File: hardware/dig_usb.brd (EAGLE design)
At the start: 146.1 x 102.6 mm, 157 parts, among them IC1 AT90USB1287-AU, IC202 DS1337S, IC203 MAX487CSA, IC204 74HC166D, IC301 LTV-356T, IC302 LTV-356T, IC303 LTV-356T, IC304 LTV-356T, IC305 LTV-356T, IC306 LTV-356T, IC307 LTV-356T, IC308 LTV-356T, K401 S202S02, K402 S202S02, K403 S202S02, K404 S202S02, K405 S202S02, K406 S202S02, K407 S202S02, K408 S202S02, Q1 16MHz, Q201 32,768kHz, T301 BCR191, T302 BCR191, T303 BCR191, T304 BCR191, T305 BCR191, T306 BCR191, T307 BCR191, T308 BCR191, X101 RIA-73-02, X201 ISP, X202 RIA-73-02, X301 RIA-73-02, X302 RIA-73-02, X303 RIA-73-02, X304 RIA-73-02, X305 RIA-73-02, X401 RIA-73-02, X402 RIA-73-02, X403 RIA-73-02, X404 RIA-73-02, X405 RIA-73-02

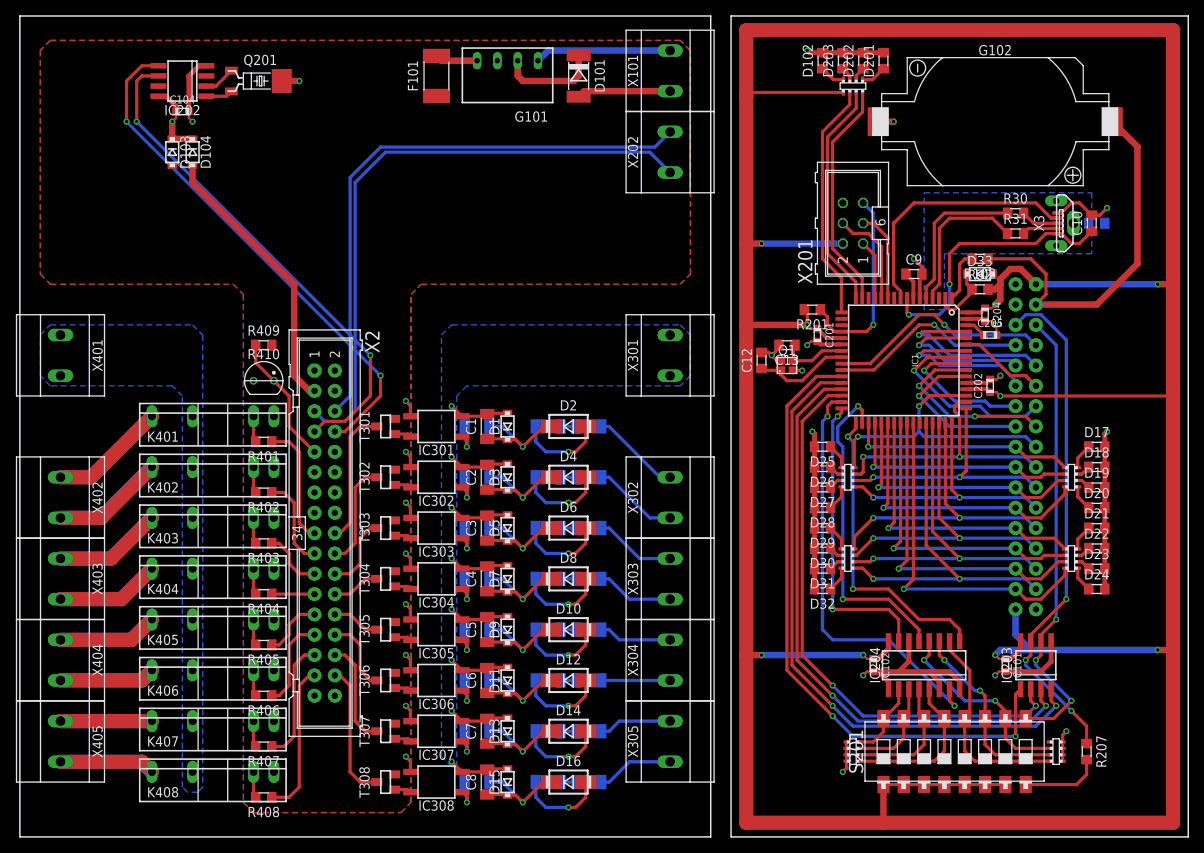
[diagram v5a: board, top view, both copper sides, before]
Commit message: Padgröße bei Wannenstecker für dig_usb angepasst
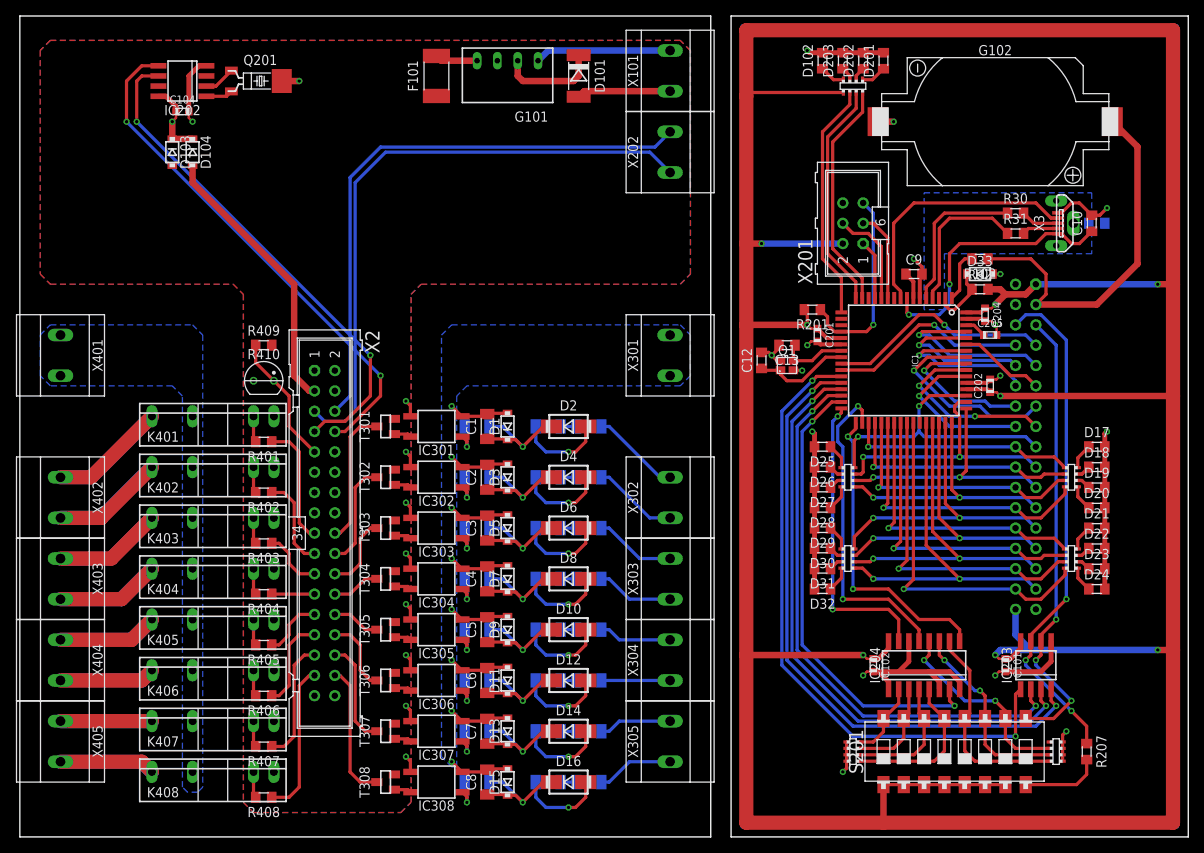
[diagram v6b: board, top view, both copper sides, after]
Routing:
- net C1: track 52.9 -> 57.6 mm
- net +5V: track 474.8 -> 472.4 mm, vias 9 -> 8
- net RXD: track 79.5 -> 80.0 mm
- net TE: track 74.8 -> 75.3 mm
- net RE: track 70.7 -> 71.2 mm
- net TXD: track 79.0 -> 79.5 mm
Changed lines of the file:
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@@
 <contactref element="X2" pad="33"/>
 <contactref element="D33" pad="A"/>
-<wire x1="121.665" y1="69.85" x2="120.65" y2="69.85" width="0.4064" layer="1"/>
-<via x="120.65" y="69.85" extent="1-16" drill="0.4"/>
+<wire x1="121.665" y1="69.85" x2="122.555" y2="69.85" width="0.4064" layer="1"/>
+<via x="122.555" y="69.85" extent="1-16" drill="0.4"/>
 <contactref element="X2" pad="4"/>
 <contactref element="G102" pad="-"/>
@@
 <wire x1="105.88" y1="21.755" x2="105.41" y2="22.225" width="0.3048" layer="1"/>
 <via x="121.92" y="22.225" extent="1-16" drill="0.4"/>
-<via x="105.41" y="22.225" extent="1-16" drill="0.4"/>
 <wire x1="90.805" y1="100.33" x2="144.145" y2="100.33" width="1.778" layer="1"/>
 <wire x1="144.145" y1="100.33" x2="144.145" y2="68.58" width="1.778" layer="1"/>
@@
 <wire x1="120.135" y1="65.055" x2="120.65" y2="65.57" width="0.508" layer="1"/>
 <contactref element="R29" pad="4B"/>
-<wire x1="105.41" y1="22.225" x2="92.71" y2="22.225" width="0.8128" layer="16"/>
-<wire x1="92.71" y1="22.225" x2="90.805" y2="22.225" width="0.8128" layer="1"/>
-<via x="92.71" y="22.225" extent="1-16" drill="0.4"/>
+<wire x1="105.41" y1="22.225" x2="90.805" y2="22.225" width="0.8128" layer="1"/>
 <wire x1="121.92" y1="22.225" x2="122.555" y2="22.86" width="0.8128" layer="16"/>
 <wire x1="122.555" y1="22.86" x2="126.365" y2="22.86" width="0.8128" layer="16"/>
@@
 <contactref element="D103" pad="A"/>
 <wire x1="124.46" y1="24.765" x2="124.46" y2="27.94" width="0.8128" layer="16"/>
-<wire x1="127" y1="68.58" x2="125.095" y2="70.485" width="0.8128" layer="1"/>
-<wire x1="125.095" y1="70.485" x2="123.825" y2="70.485" width="0.8128" layer="1"/>
-<wire x1="123.825" y1="70.485" x2="122.555" y2="69.215" width="0.8128" layer="1"/>
-<wire x1="122.555" y1="69.215" x2="122.555" y2="68.58" width="0.8128" layer="1"/>
-<wire x1="122.555" y1="68.58" x2="122.555" y2="66.675" width="0.8128" layer="1"/>
-<wire x1="122.555" y1="66.675" x2="121.92" y2="66.04" width="0.8128" layer="1"/>
-<wire x1="121.015" y1="67.945" x2="121.92" y2="67.945" width="0.8128" layer="1"/>
-<wire x1="121.92" y1="67.945" x2="122.555" y2="68.58" width="0.8128" layer="1"/>
+<wire x1="123.19" y1="67.31" x2="121.92" y2="66.04" width="0.8128" layer="1"/>
 <wire x1="144.145" y1="68.58" x2="142.24" y2="68.58" width="0.8128" layer="1"/>
 <via x="142.24" y="68.58" extent="1-16" drill="0.4"/>
 <wire x1="142.24" y1="68.58" x2="127" y2="68.58" width="0.8128" layer="16"/>
-<wire x1="122.555" y1="54.61" x2="144.145" y2="54.61" width="0.4064" layer="1"/>
+<wire x1="122.555" y1="54.61" x2="144.145" y2="54.61" width="0.8128" layer="1"/>
 <wire x1="122.085" y1="55.08" x2="122.555" y2="54.61" width="0.3048" layer="1"/>
 <polygon width="0.4064" layer="1">
@@
 <vertex x="26.67" y="68.58"/>
 </polygon>
+<wire x1="123.19" y1="67.31" x2="125.73" y2="67.31" width="0.8128" layer="1"/>
+<wire x1="125.73" y1="67.31" x2="127" y2="68.58" width="0.8128" layer="1"/>
+<wire x1="121.015" y1="67.945" x2="122.555" y2="67.945" width="0.8128" layer="1"/>
+<wire x1="122.555" y1="67.945" x2="123.19" y2="67.31" width="0.8128" layer="1"/>
+<via x="105.41" y="22.225" extent="1-16" drill="0.4"/>
 <wire x1="52.07" y1="92.115" x2="90.805" y2="92.075" width="0" layer="19" extent="1-1"/>
 </signal>
@@
 <contactref element="IC204" pad="7"/>
 <contactref element="IC1" pad="31"/>
-<via x="100.965" y="52.07" extent="1-16" drill="0.4"/>
-<wire x1="100.965" y1="52.07" x2="100.33" y2="51.435" width="0.4064" layer="16"/>
-<wire x1="100.33" y1="51.435" x2="100.33" y2="25.4" width="0.4064" layer="16"/>
-<wire x1="100.33" y1="25.4" x2="101.6" y2="24.13" width="0.4064" layer="16"/>
-<wire x1="101.6" y1="24.13" x2="108.585" y2="24.13" width="0.4064" layer="16"/>
+<via x="99.06" y="51.435" extent="1-16" drill="0.4"/>
 <via x="116.84" y="15.875" extent="1-16" drill="0.4"/>
 <wire x1="116.84" y1="15.875" x2="116.205" y2="16.51" width="0.4064" layer="1"/>
 <wire x1="116.205" y1="16.51" x2="116.205" y2="17.955" width="0.4064" layer="1"/>
 <wire x1="102.69" y1="53.855" x2="101.48" y2="53.855" width="0.4064" layer="1"/>
-<wire x1="101.48" y1="53.855" x2="100.965" y2="53.34" width="0.4064" layer="1"/>
-<wire x1="100.965" y1="53.34" x2="100.965" y2="52.07" width="0.4064" layer="1"/>
-<wire x1="108.585" y1="24.13" x2="116.84" y2="15.875" width="0.4064" layer="16"/>
+<wire x1="101.48" y1="53.855" x2="99.06" y2="51.435" width="0.4064" layer="1"/>
+<wire x1="99.06" y1="51.435" x2="97.79" y2="50.165" width="0.4064" layer="16"/>
+<wire x1="97.79" y1="50.165" x2="97.79" y2="23.495" width="0.4064" layer="16"/>
+<wire x1="97.79" y1="23.495" x2="105.41" y2="15.875" width="0.4064" layer="16"/>
+<wire x1="105.41" y1="15.875" x2="116.84" y2="15.875" width="0.4064" layer="16"/>
 </signal>
 <signal name="!R">
@@
 <wire x1="128.905" y1="16.51" x2="129.54" y2="15.875" width="0.4064" layer="1"/>
 <via x="129.54" y="15.875" extent="1-16" drill="0.4"/>
-<wire x1="96.52" y1="20.955" x2="101.6" y2="15.875" width="0.4064" layer="1"/>
-<via x="101.6" y="15.875" extent="1-16" drill="0.4"/>
-<wire x1="101.6" y1="15.875" x2="104.14" y2="13.335" width="0.4064" layer="16"/>
+<wire x1="95.885" y1="21.59" x2="104.14" y2="13.335" width="0.4064" layer="16"/>
 <wire x1="104.14" y1="13.335" x2="127" y2="13.335" width="0.4064" layer="16"/>
 <wire x1="127" y1="13.335" x2="129.54" y2="15.875" width="0.4064" layer="16"/>
 <wire x1="102.69" y1="56.255" x2="100.07" y2="56.255" width="0.4064" layer="1"/>
-<wire x1="100.07" y1="56.255" x2="96.52" y2="52.705" width="0.4064" layer="1"/>
-<wire x1="96.52" y1="52.705" x2="96.52" y2="20.955" width="0.4064" layer="1"/>
+<wire x1="100.07" y1="56.255" x2="99.06" y2="55.245" width="0.4064" layer="1"/>
+<wire x1="99.06" y1="55.245" x2="95.885" y2="52.07" width="0.4064" layer="16"/>
+<wire x1="95.885" y1="52.07" x2="95.885" y2="21.59" width="0.4064" layer="16"/>
+<via x="99.06" y="55.245" extent="1-16" drill="0.4"/>
 </signal>
 <signal name="RXD">
 <contactref element="IC203" pad="1"/>
 <contactref element="IC1" pad="27"/>
-<wire x1="95.885" y1="20.32" x2="101.6" y2="14.605" width="0.4064" layer="1"/>
+<wire x1="95.25" y1="20.955" x2="104.14" y2="12.065" width="0.4064" layer="16"/>
 <wire x1="125.095" y1="17.955" x2="124.46" y2="17.32" width="0.4064" layer="1"/>
 <wire x1="124.46" y1="17.32" x2="124.46" y2="12.065" width="0.4064" layer="1"/>
 <via x="124.46" y="12.065" extent="1-16" drill="0.4"/>
 <wire x1="124.46" y1="12.065" x2="104.14" y2="12.065" width="0.4064" layer="16"/>
-<wire x1="104.14" y1="12.065" x2="101.6" y2="14.605" width="0.4064" layer="16"/>
-<via x="101.6" y="14.605" extent="1-16" drill="0.4"/>
 <wire x1="102.69" y1="57.055" x2="99.6" y2="57.055" width="0.4064" layer="1"/>
-<wire x1="99.6" y1="57.055" x2="95.885" y2="53.34" width="0.4064" layer="1"/>
-<wire x1="95.885" y1="53.34" x2="95.885" y2="20.32" width="0.4064" layer="1"/>
+<wire x1="99.6" y1="57.055" x2="99.06" y2="56.515" width="0.4064" layer="1"/>
+<wire x1="99.06" y1="56.515" x2="95.25" y2="52.705" width="0.4064" layer="16"/>
+<wire x1="95.25" y1="52.705" x2="95.25" y2="20.955" width="0.4064" layer="16"/>
+<via x="99.06" y="56.515" extent="1-16" drill="0.4"/>
 </signal>
 <signal name="TE">
@@
 <wire x1="127.635" y1="16.51" x2="128.27" y2="15.875" width="0.4064" layer="1"/>
 <via x="128.27" y="15.875" extent="1-16" drill="0.4"/>
-<wire x1="97.155" y1="21.59" x2="101.6" y2="17.145" width="0.4064" layer="1"/>
-<via x="101.6" y="17.145" extent="1-16" drill="0.4"/>
-<wire x1="101.6" y1="17.145" x2="104.775" y2="13.97" width="0.4064" layer="16"/>
+<wire x1="96.52" y1="22.225" x2="104.775" y2="13.97" width="0.4064" layer="16"/>
 <wire x1="104.775" y1="13.97" x2="126.365" y2="13.97" width="0.4064" layer="16"/>
 <wire x1="126.365" y1="13.97" x2="128.27" y2="15.875" width="0.4064" layer="16"/>
 <wire x1="102.69" y1="55.455" x2="100.54" y2="55.455" width="0.4064" layer="1"/>
-<wire x1="100.54" y1="55.455" x2="97.155" y2="52.07" width="0.4064" layer="1"/>
-<wire x1="97.155" y1="52.07" x2="97.155" y2="21.59" width="0.4064" layer="1"/>
+<wire x1="100.54" y1="55.455" x2="99.06" y2="53.975" width="0.4064" layer="1"/>
+<wire x1="99.06" y1="53.975" x2="96.52" y2="51.435" width="0.4064" layer="16"/>
+<wire x1="96.52" y1="51.435" x2="96.52" y2="22.225" width="0.4064" layer="16"/>
+<via x="99.06" y="53.975" extent="1-16" drill="0.4"/>
 </signal>
 <signal name="RE">
@@
 <wire x1="126.365" y1="16.51" x2="127" y2="15.875" width="0.4064" layer="1"/>
 <via x="127" y="15.875" extent="1-16" drill="0.4"/>
-<wire x1="97.79" y1="22.225" x2="101.6" y2="18.415" width="0.4064" layer="1"/>
-<via x="101.6" y="18.415" extent="1-16" drill="0.4"/>
-<wire x1="101.6" y1="18.415" x2="105.41" y2="14.605" width="0.4064" layer="16"/>
+<wire x1="97.155" y1="22.86" x2="105.41" y2="14.605" width="0.4064" layer="16"/>
 <wire x1="105.41" y1="14.605" x2="125.73" y2="14.605" width="0.4064" layer="16"/>
 <wire x1="125.73" y1="14.605" x2="127" y2="15.875" width="0.4064" layer="16"/>
 <wire x1="102.69" y1="54.655" x2="101.01" y2="54.655" width="0.4064" layer="1"/>
-<wire x1="101.01" y1="54.655" x2="97.79" y2="51.435" width="0.4064" layer="1"/>
-<wire x1="97.79" y1="51.435" x2="97.79" y2="22.225" width="0.4064" layer="1"/>
+<wire x1="101.01" y1="54.655" x2="99.06" y2="52.705" width="0.4064" layer="1"/>
+<wire x1="99.06" y1="52.705" x2="97.155" y2="50.8" width="0.4064" layer="16"/>
+<wire x1="97.155" y1="50.8" x2="97.155" y2="22.86" width="0.4064" layer="16"/>
+<via x="99.06" y="52.705" extent="1-16" drill="0.4"/>
 </signal>
 <signal name="N$62">

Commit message: Widerstandsarrays für LEDs gegen CHIP0805 bei dig_usb getauscht
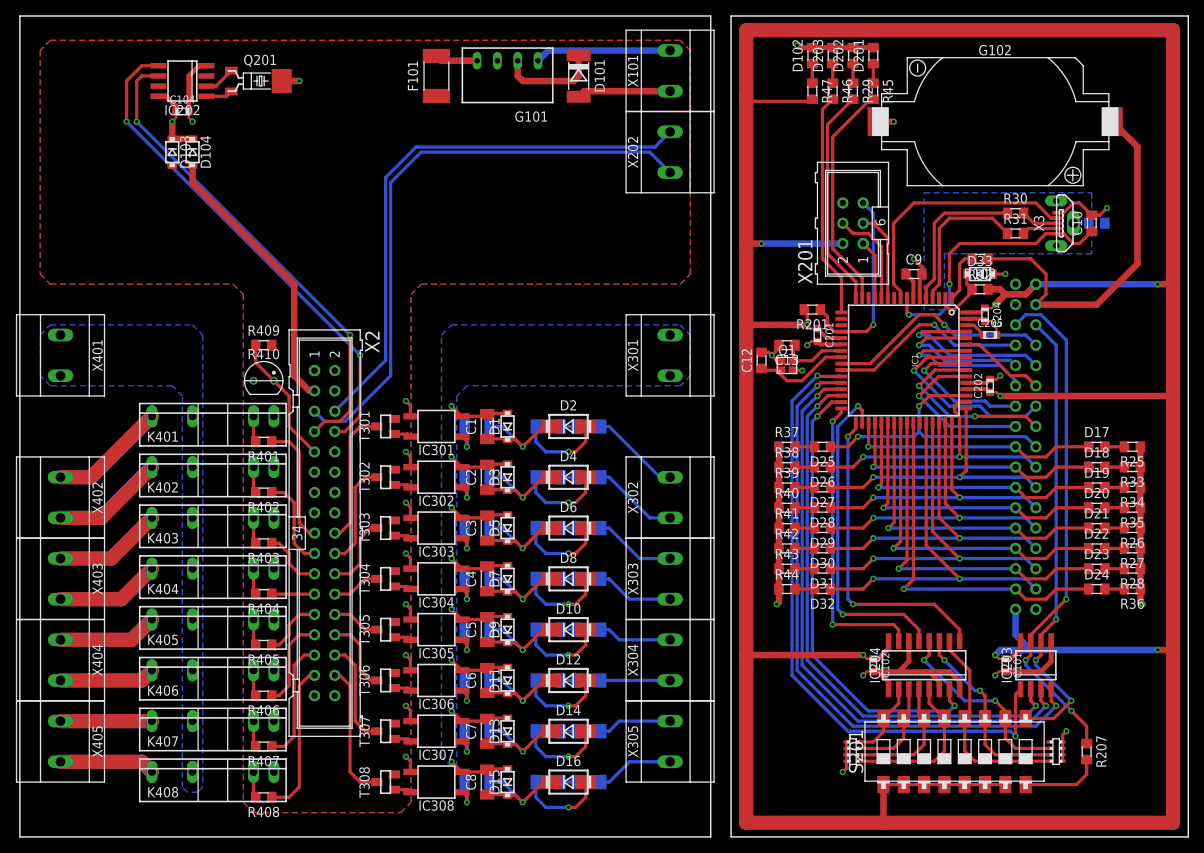
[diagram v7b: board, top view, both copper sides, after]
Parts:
- added R33, R34, R35, R36, R37, R38, R39, R40, R41, R42, R43, R44, R45, R46, R47: 1,5kΩ, passiv:CHIP_0805
- R25, R26, R27, R28, R29: device widerstandsnetzwerk:1206 -> passiv:CHIP_0805
- moved R27 36.7 mm to (139.1, 35.6), turned to 180 degrees
- moved R28 35.6 mm to (139.1, 33.0), turned to 180 degrees
- moved R26 8.52 mm to (139.1, 38.1), turned to 180 degrees
- moved R25 8.52 mm to (139.1, 48.3), turned to 180 degrees
- moved D203 1.42 mm to (101.6, 97.2)
- moved D102 1.42 mm to (99.1, 97.2)
- moved D201 1.42 mm to (106.7, 97.2)
- moved D202 1.42 mm to (104.1, 97.2)
- moved R29 0.64 mm to (104.1, 92.7), turned to 270 degrees
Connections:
- net +5V: now also R47.2; no longer R29.4B
- net GND: now also R25.1, R26.1, R27.1, R28.1, R33.1, R34.1, R35.1, R36.1, R37.1, R38.1, R39.1, R40.1, R41.1, R42.1, R43.1, R44.1; no longer D17.2, D18.2, D19.2, D20.2, D21.2, D22.2, D23.2, D24.2, D25.2, D26.2, D27.2, D28.2, D29.2, D30.2, D31.2, D32.2
- net IN0: now also D17.1; no longer R25.1A
- net IN1: now also D18.1; no longer R25.2A
- net IN2: now also D19.1; no longer R25.3A
- net IN3: now also D20.1; no longer R25.4A
- net IN4: now also D21.1; no longer R26.1A
- net IN5: now also D22.1; no longer R26.2A
- net IN6: now also D23.1; no longer R26.3A
- net IN7: now also D24.1; no longer R26.4A
- net LED1: now also R45.2; no longer R29.1B
- net LED2: now also R29.2; no longer R29.2B
- net LED3: now also R46.2; no longer R29.3B
- net N$102: now also D17.2, R25.2; no longer D17.1, R25.1B
- net N$103: now also D18.2, R33.2; no longer D18.1, R25.2B
- net N$104: now also D19.2, R34.2; no longer D19.1, R25.3B
- net N$105: now also D20.2, R35.2; no longer D20.1, R25.4B
- net N$106: now also D21.2, R26.2; no longer D21.1, R26.1B
- net N$107: now also D22.2, R27.2; no longer D22.1, R26.2B
- net N$108: now also D23.2, R28.2; no longer D23.1, R26.3B
- net N$109: now also D24.2, R36.2; no longer D24.1, R26.4B
- net N$110: now also D25.2, R37.2; no longer D25.1, R27.1A
- net N$111: now also D26.2, R38.2; no longer D26.1, R27.2A
- net N$112: now also D27.2, R39.2; no longer D27.1, R27.3A
- net N$113: now also D28.2, R40.2; no longer D28.1, R27.4A
- net N$114: now also D29.2, R41.2; no longer D29.1, R28.1A
- net N$115: now also D30.2, R42.2; no longer D30.1, R28.2A
- net N$116: now also D31.2, R43.2; no longer D31.1, R28.3A
- net N$117: now also D32.2, R44.2; no longer D32.1, R28.4A
- net N$4: now also R46.1; no longer R29.3A
- net N$44: now also R47.1; no longer R29.4A
- net N$62: now also R45.1; no longer R29.1A
- net N$63: now also R29.1; no longer R29.2A
- net OUT0: now also D25.1; no longer R27.1B
- net OUT1: now also D26.1; no longer R27.2B
- net OUT2: now also D27.1; no longer R27.3B
- net OUT3: now also D28.1; no longer R27.4B
- net OUT4: now also D29.1; no longer R28.1B
- net OUT5: now also D30.1; no longer R28.2B
- net OUT6: now also D31.1; no longer R28.3B
- net OUT7: now also D32.1; no longer R28.4B
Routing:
- net OUT2: track 32.3 -> 35.7 mm
- net OUT6: track 41.8 -> 45.1 mm
- net IN1: track 30.3 -> 33.6 mm
- net IN5: track 38.2 -> 41.5 mm
- net +5V: track 472.4 -> 469.1 mm
- net OUT7: track 45.0 -> 48.0 mm
- net OUT3: track 33.5 -> 36.5 mm
- net IN4: track 36.6 -> 39.5 mm
- net IN0: track 28.7 -> 31.6 mm
- net OUT5: track 39.6 -> 42.2 mm
- net IN6: track 40.9 -> 43.5 mm
- net IN2: track 33.0 -> 35.6 mm
- net N$133: track 72.4 -> 69.8 mm
- net N$134: track 76.7 -> 74.1 mm
- net N$131: track 63.3 -> 60.8 mm
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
